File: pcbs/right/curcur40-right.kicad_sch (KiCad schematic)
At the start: 88 parts, among them U1 PMW3360DM-T2QU, U2 TLV74318PDBVR

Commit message: fix(pcb): update spacer holes to 3.25mm, shift SMDSW1/2, remove 0.4mm NPTH hole, and sync U1/CKW12 attributes
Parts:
- U1: now left out of the parts list
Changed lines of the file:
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@@
 		(body_style 1)
 		(exclude_from_sim no)
-		(in_bom yes)
+		(in_bom no)
 		(on_board yes)
-		(in_pos_files yes)
+		(in_pos_files no)
 		(dnp no)
 		(property "Reference" "U1"

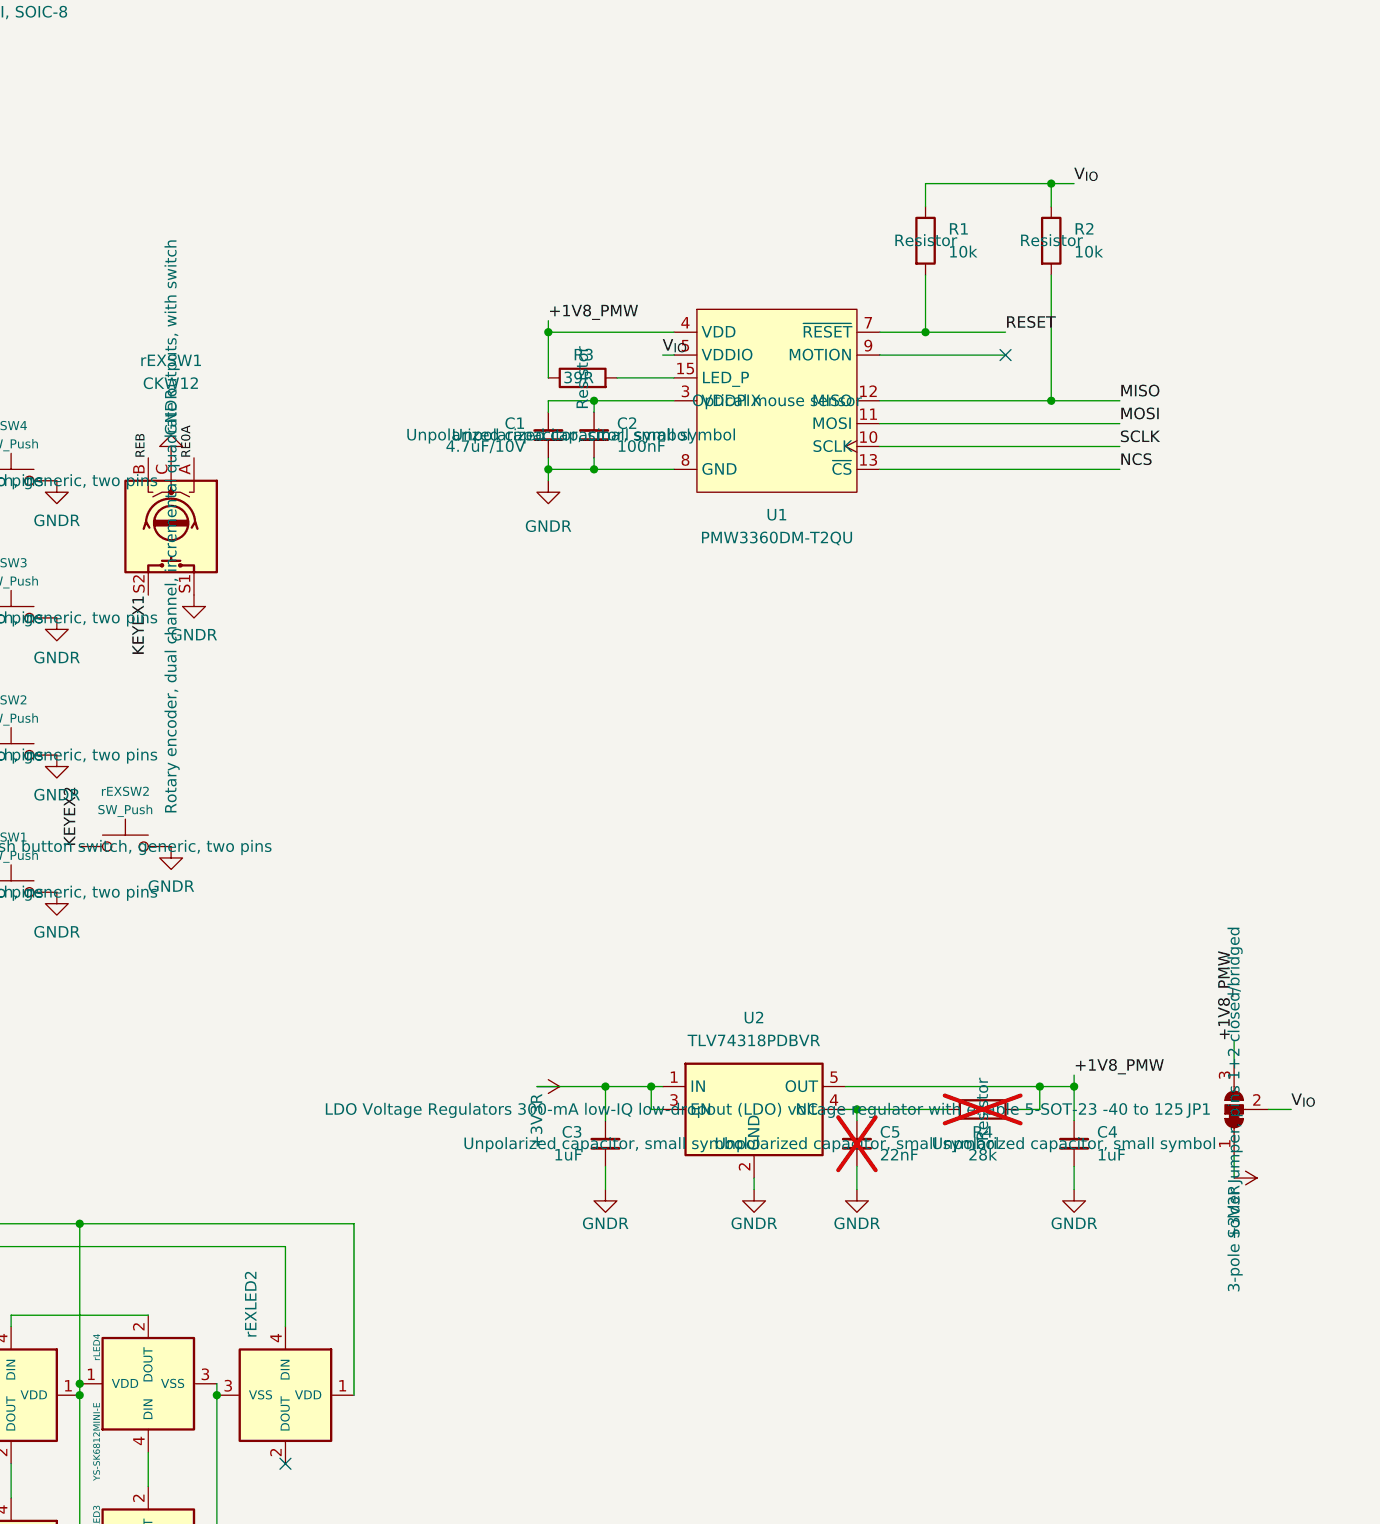
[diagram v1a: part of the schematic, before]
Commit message: feat(pcb): separate pmw3360 sensor PCB with JST SH 6-pin connector and add symmetric thumb mounting holes L5/R5
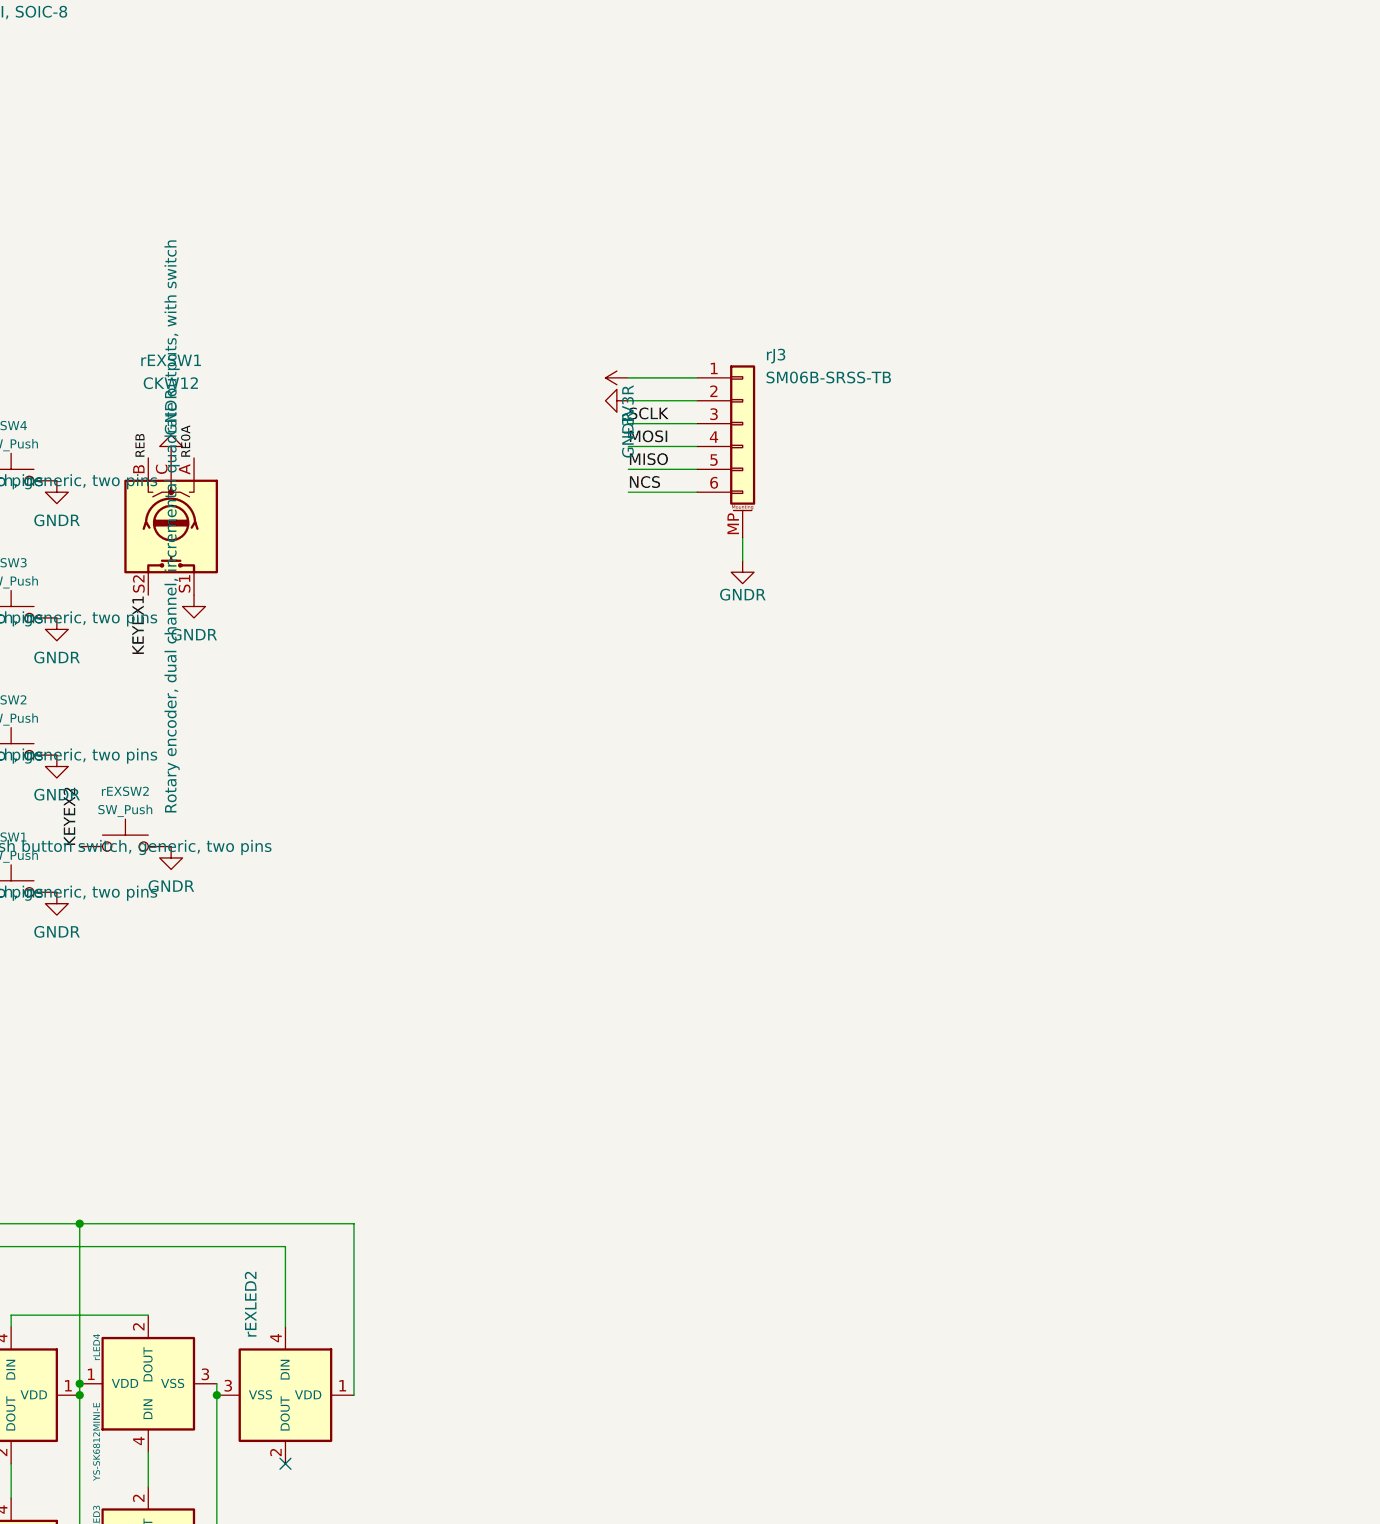
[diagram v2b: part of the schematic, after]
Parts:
- removed C1: 4.7uF/10V, Capacitor_SMD:C_0603_1608Metric_Pad1.08x0.95mm_HandSolder, symbol Device:C_Small
- removed C2: 100nF, Capacitor_SMD:C_0603_1608Metric_Pad1.08x0.95mm_HandSolder, symbol Device:C_Small
- removed C3, C4: 1uF, Capacitor_SMD:C_0603_1608Metric_Pad1.08x0.95mm_HandSolder, symbol Device:C_Small
- removed C5: 22nF, Capacitor_SMD:C_0603_1608Metric_Pad1.08x0.95mm_HandSolder, symbol Device:C_Small
- removed JP1: SolderJumper_3_Bridged12, Jumper:SolderJumper-3_P1.3mm_Bridged12_RoundedPad1.0x1.5mm_NumberLabels, symbol Jumper:SolderJumper_3_Bridged12
- removed R1, R2: 10k, Resistor_SMD:R_0603_1608Metric_Pad0.98x0.95mm_HandSolder, symbol Device:R
- removed R3: 39R, Resistor_SMD:R_0603_1608Metric_Pad0.98x0.95mm_HandSolder, symbol Device:R
- removed R4: 28k, Resistor_SMD:R_0603_1608Metric_Pad0.98x0.95mm_HandSolder, symbol Device:R
- removed U1: PMW3360DM-T2QU, kbd:PMW3360DM-T2QU_16Pin, symbol PMW3360_PCB:PMW3360DM-T2QU
- removed U2: TLV74318PDBVR, Package_TO_SOT_SMD:SOT-23-5, symbol PMW3360_PCB:TLV74318PDBVR
- added rJ3: SM06B-SRSS-TB, Connector_JST:JST_SH_SM06B-SRSS-TB_1x06-1MP_P1.00mm_Horizontal, symbol Connector_Generic_MountingPin:Conn_01x06_MountingPin
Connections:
- net +3V3R: now also rJ3.1 (Pin_1)
- net GNDR: now also rJ3.2 (Pin_2), rJ3.MP (MountPin)
- net MISO: now also rJ3.5 (Pin_5)
- net MOSI: now also rJ3.4 (Pin_4)
- net NCS: now also rJ3.6 (Pin_6)
- net SCLK: now also rJ3.3 (Pin_3)
- no-connect marks 4 -> 3

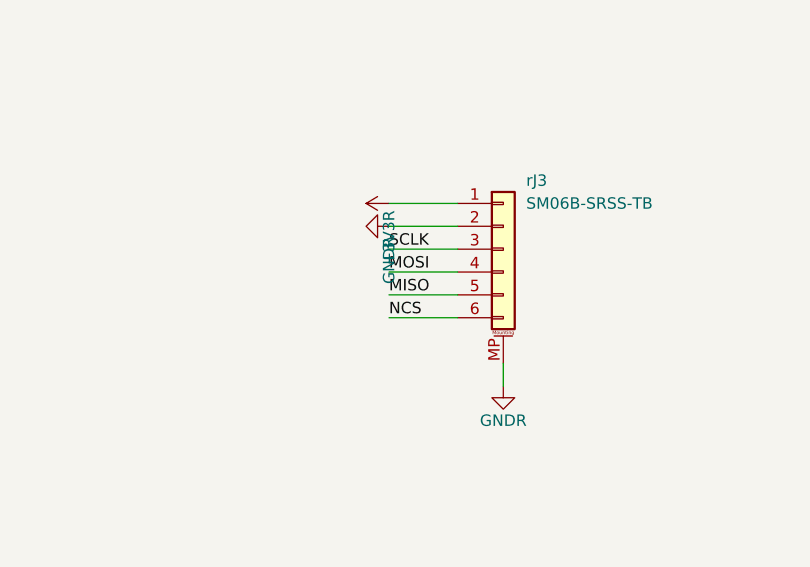
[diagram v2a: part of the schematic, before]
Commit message: feat(pcb): shift rJ3 east to (46.5, 63.0) for rSW1 socket clearance and align N-S pin order with J1
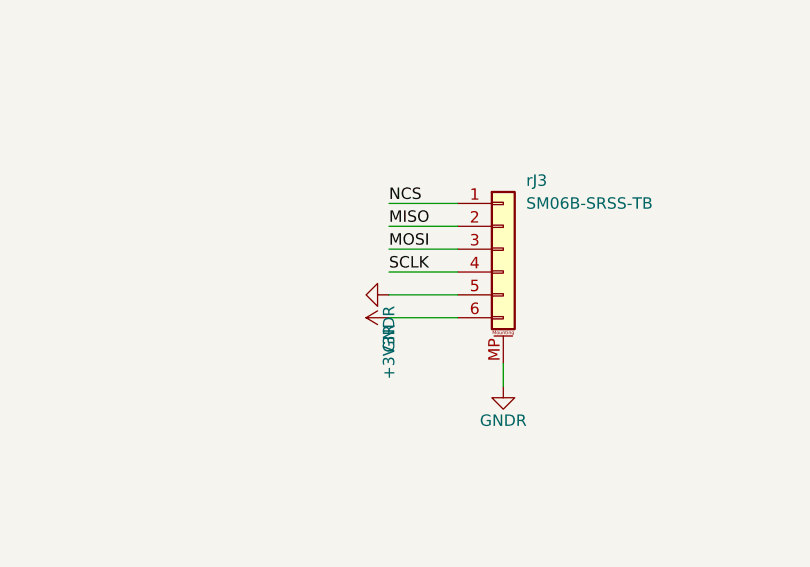
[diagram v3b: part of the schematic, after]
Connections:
- net +3V3R: now also rJ3.6 (Pin_6); no longer rJ3.1 (Pin_1)
- net GNDR: now also rJ3.5 (Pin_5); no longer rJ3.2 (Pin_2)
- net MISO: now also rJ3.2 (Pin_2); no longer rJ3.5 (Pin_5)
- net MOSI: now also rJ3.3 (Pin_3); no longer rJ3.4 (Pin_4)
- net NCS: now also rJ3.1 (Pin_1); no longer rJ3.6 (Pin_6)
- net SCLK: now also rJ3.4 (Pin_4); no longer rJ3.3 (Pin_3)
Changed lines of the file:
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@@
 	(symbol
 		(lib_id "kbd:+3V3R")
-		(at 317.5 96.52 90)
+		(at 317.5 109.22 90)
 		(unit 1)
 		(exclude_from_sim no)
@@
 		(fields_autoplaced yes)
 		(property "Reference" "#PWR0201"
-			(at 317.5 102.86999999999999 0)
+			(at 317.5 115.57 0)
 			(effects
 				(font
@@
 		)
 		(property "Value" "+3V3R"
-			(at 317.5 100.33 0)
+			(at 317.5 113.03 0)
 			(effects
 				(font
@@
 		)
 		(property "Footprint" ""
-			(at 317.5 96.52 0)
+			(at 317.5 109.22 0)
 			(effects
 				(font
@@
 		)
 		(property "Datasheet" ""
-			(at 317.5 96.52 0)
+			(at 317.5 109.22 0)
 			(effects
 				(font
@@
 		)
 		(property "Description" ""
-			(at 317.5 96.52 0)
+			(at 317.5 109.22 0)
 			(effects
 				(font
@@
 	(symbol
 		(lib_id "kbd:GNDR")
-		(at 317.5 99.06 270)
+		(at 317.5 106.68 270)
 		(unit 1)
 		(exclude_from_sim no)
@@
 		(fields_autoplaced yes)
 		(property "Reference" "#PWR0202"
-			(at 317.5 105.41 0)
+			(at 317.5 113.03 0)
 			(effects
 				(font
@@
 		)
 		(property "Value" "GNDR"
-			(at 317.5 102.87 0)
+			(at 317.5 110.49 0)
 			(effects
 				(font
@@
 		)
 		(property "Footprint" ""
-			(at 317.5 99.06 0)
+			(at 317.5 106.68 0)
 			(effects
 				(font
@@
 		)
 		(property "Datasheet" ""
-			(at 317.5 99.06 0)
+			(at 317.5 106.68 0)
 			(effects
 				(font
@@
 		)
 		(property "Description" ""
-			(at 317.5 99.06 0)
+			(at 317.5 106.68 0)
 			(effects
 				(font
@@
 	)
 	(label "SCLK"
+		(at 317.5 104.14 0)
+		(effects
+			(font
+				(size 1.27 1.27)
+			)
+			(justify left bottom)
+		)
+	)
+	(label "MOSI"
 		(at 317.5 101.6 0)
 		(effects
@@
 		)
 	)
-	(label "MOSI"
-		(at 317.5 104.14 0)
+	(label "MISO"
+		(at 317.5 99.06 0)
 		(effects
 			(font
@@
 		)
 	)
-	(label "MISO"
-		(at 317.5 106.68 0)
-		(effects
-			(font
-				(size 1.27 1.27)
-			)
-			(justify left bottom)
-		)
-	)
 	(label "NCS"
-		(at 317.5 109.22 0)
-		(effects
-			(font
+		(at 317.5 96.52 0)
+		(effects
+			(font

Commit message: fix(bom,pcb): update JST SH 6-pin connector LCSC part number from C160404 to C160405
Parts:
- rJ3: LCSC C160404 -> C160405
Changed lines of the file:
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@@
 			)
 		)
-		(property "LCSC" "C160404"
+		(property "LCSC" "C160405"
 			(at 330.2 101.6 0)
 			(effects

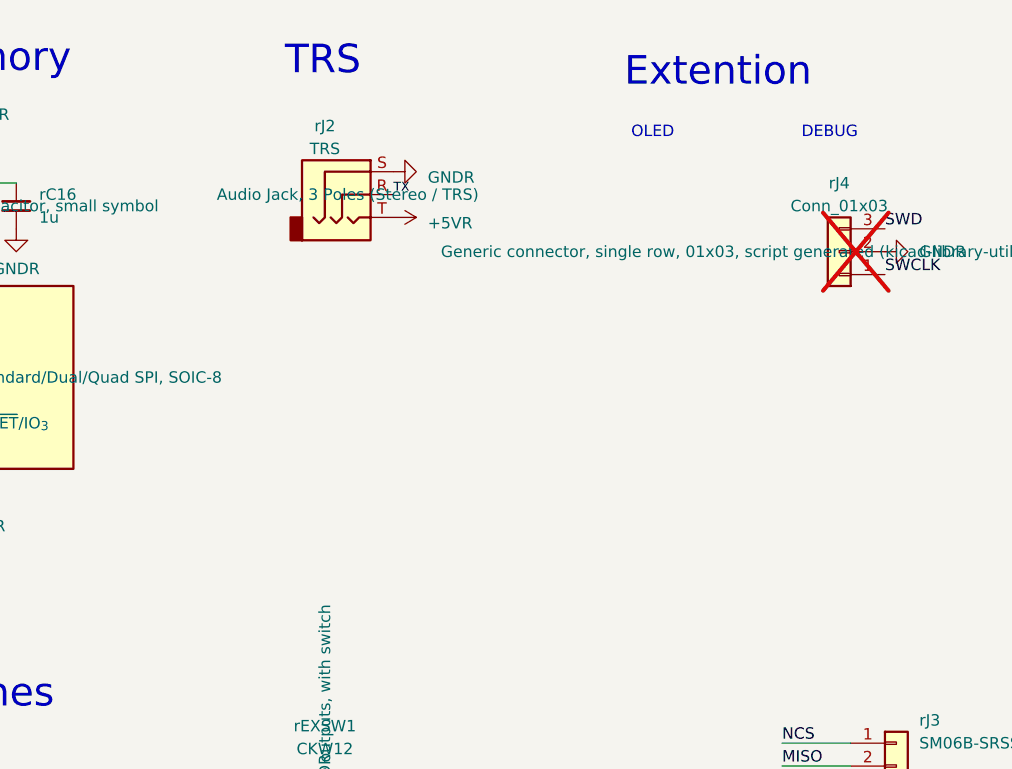
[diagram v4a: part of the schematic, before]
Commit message: feat(pcb): replace split TRRS jack with USB-C receptacle and ESD/series protection
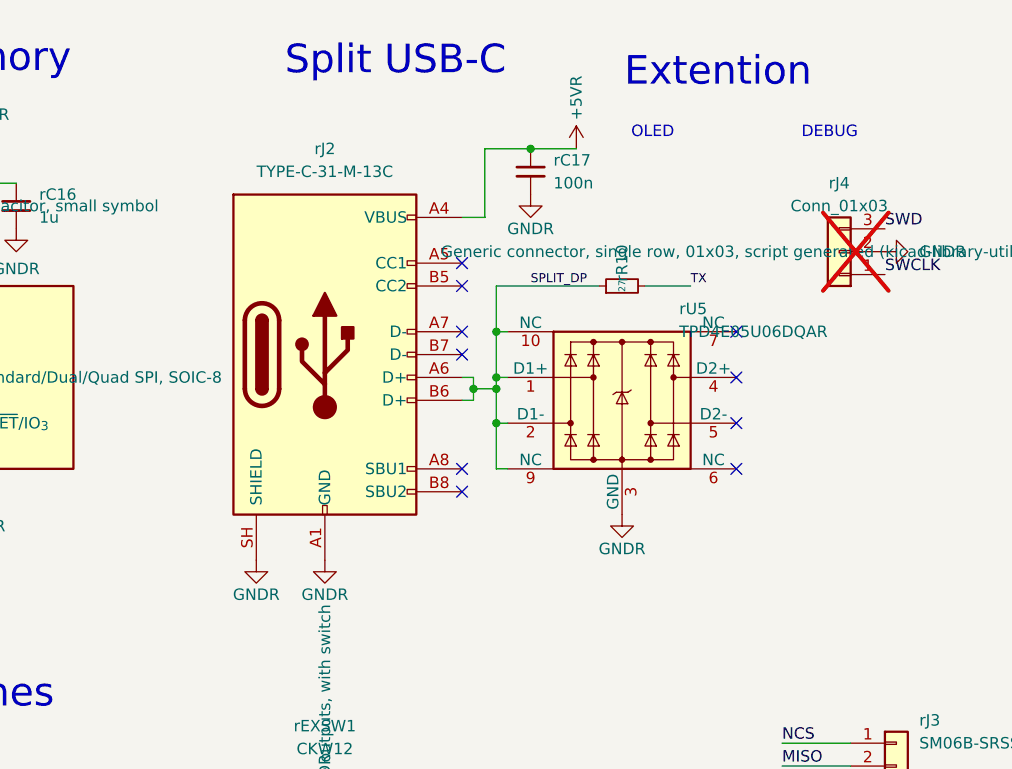
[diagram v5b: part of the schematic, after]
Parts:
- added rC17: 100n, Capacitor_SMD:C_0402_1005Metric, symbol Device:C_Small
- added rR10: 27, Resistor_SMD:R_0402_1005Metric, symbol Device:R_Small
- added rU5: TPD4E05U06DQAR, Package_SON:USON-10_2.5x1.0mm_P0.5mm, symbol Power_Protection:TPD4EUSB30
- rJ2: value TRS -> TYPE-C-31-M-13C; footprint kbd:Jack_PJ-398A-5A_PJ-399B-6A -> kbd:USB_C_Receptacle_TYPE-C-31-M-13C; symbol Connector_Audio:AudioJack3 -> Connector:USB_C_Receptacle_USB2.0_16P; JLCPCB Part # C128994 -> C2848620
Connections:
- net +5VR: now also rJ2.A4 (VBUS), rJ2.A9 (VBUS), rJ2.B4 (VBUS), rJ2.B9 (VBUS), rC17.1; no longer rJ2.T
- net GNDR: now also rJ2.A1 (GND), rJ2.A12 (GND), rJ2.B1 (GND), rJ2.B12 (GND), rJ2.SH (SHIELD), rC17.2, rU5.3 (GND), rU5.8 (GND); no longer rJ2.S
- net TX: now also rR10.2; no longer rJ2.R
- new net SPLIT_DP: rJ2.A6 (D+), rJ2.B6 (D+), rR10.1, rU5.1 (D1+), rU5.10 (NC), rU5.2 (D1-), rU5.9 (NC)
- no-connect marks 3 -> 13
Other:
- note added: "Split USB-C"
- note removed: "TRS"
